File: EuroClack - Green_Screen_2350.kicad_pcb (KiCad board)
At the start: 4 copper layers, 99.1 x 110 mm, 272 parts, among them J1 C2982548, J10 CV_OUT_4, J11 C7471773, J12 DISPLAY_CONNECTOR, J13 CV_GATE_IN_4, J14 AUDIO_OUT_1, J15 AUDIO_IN_1, J16 USB_C_Receptacle_USB2.0_14P, J17 USB_HOST, J18 Eurorack 10 pin socket, J19 C7470101, J2 AUDIO_IN_2, J20 STEMMA_QT, J21 C2856837, J22 C2856837, J23 CV_GATE_IN3, J24 CV_GATE_IN_4, J25 SM03B-SRSS-TB, J26 CV_OUT_3, J27 CV_OUT_4, J28 C2881890, J29 C7470089, J3 CV_GATE_IN_1, J4 CV_GATE_IN_2, J5 CV_GATE_IN3, J6 AUDIO_OUT_2, J7 CV_OUT_1, J8 CV_OUT_2, J9 CV_OUT_3, Q1 A3400A, Q2 A3401A, Q3 A3401A, Q4 A3400A, SW3 RotaryEncoder_Switch, SW4 RotaryEncoder_Switch, SW5 USER2, SW6 SW_Push, SW7 SW_Push, U1 RP2350_80QFN, U10 SPX3819M5-L-5-0, U11 TL072, U12 TPS54302, U13 TL072, U14 SPX3819M5-L-3-3, U15 SRAM, U16 SPX3819M5-L-3-3, U17 TL072, U18 SN74LVC1T45DCK, U19 LM393, U2 PCM5102, U20 TL072, U21 LM393, U22 SN74LVC1T45DCK, U23 TPS54302, U3 MCP4728, U4 W25Q128JVS, U5 PCM1808PWR, U6 TL072, U7 REF3033, U8 TL072, U9 SPX3819M5-L-3-3, Y1 ABM8-272-T3

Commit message: work on connectors layout
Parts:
- removed the J12 at (225.0, 54.7)
- removed PIL1, PIL2, PIL3, PIL4: SMD_SMTSO20100CTJ, green_screen:SMD_SMTSO20100CTJ
- removed the REF** at (71.5, 111.0)
- removed the REF** at (113.5, 126.5)
- removed the REF** at (225.6, 93.9)
- removed the REF** at (256.1, 96.9)
- removed the REF** at (89.5, 126.5)
- removed the REF** at (30.0, 111.0)
- removed the REF** at (71.5, 55.5)
- removed the REF** at (30.0, 55.5)
- removed the REF** at (113.5, 150.6)
- added J30: FFC, green_screen:FPC-SMD_F1004-H-08-20G-R, F.Cu at (106.3, 59.6)
- added REF**: MountingHole_2.1mm, MountingHole:MountingHole_2.1mm, F.Cu at (88.4, 111.0)
- added REF**: MountingHole_2.1mm, MountingHole:MountingHole_2.1mm, F.Cu at (93.4, 126.6)
- added REF**: MountingHole_2.2mm_M2, MountingHole:MountingHole_2.2mm_M2, F.Cu at (71.5, 55.4)
- added REF**: MountingHole_2.1mm, MountingHole:MountingHole_2.1mm, F.Cu at (129.9, 111.0)
- added REF**: MountingHole_2.2mm_M2, MountingHole:MountingHole_2.2mm_M2, F.Cu at (30.0, 111.0)
- added REF**: MountingHole_2.1mm, MountingHole:MountingHole_2.1mm, F.Cu at (88.4, 55.5)
- added REF**: MountingHole_2.2mm_M2, MountingHole:MountingHole_2.2mm_M2, F.Cu at (106.2, 100.0)
- added REF**: MountingHole_2.2mm_M2, MountingHole:MountingHole_2.2mm_M2, F.Cu at (71.5, 111.0)
- added REF**: MountingHole_2.1mm, MountingHole:MountingHole_2.1mm, F.Cu at (119.3, 126.5)
- added REF**: MountingHole_2.1mm, MountingHole:MountingHole_2.1mm, F.Cu at (129.9, 55.5)
- added REF**: MountingHole_2.1mm, MountingHole:MountingHole_2.1mm, F.Cu at (119.3, 150.6)
- added REF**: MountingHole_2.2mm_M2, MountingHole:MountingHole_2.2mm_M2, F.Cu at (30.1, 55.6)
- J12: value DISPLAY_CONNECTOR -> Pin Header
- J16: footprint Clacktronics:918-418K2022Y40000 -> green_screen:USB-C-TH_TYPE-C-USB-14P
- J17: footprint Connector_USB:USB_A_Molex_105057_Vertical -> green_screen:USB-A-SMD_AF180-13.1
- SW3, SW4: footprint Rotary_Encoder:RotaryEncoder_Alps_EC12E-Switch_Vertical_H20mm_CircularMountingHoles -> green_screen:SW-TH_EC11XXXXXXXX
- SW5, SW6, SW7: footprint green_screen:KEY-SMD_4P-L6.0-W6.0-P3.90-LS9.0 -> green_screen:SW-TH_4P-L5.0-W5.0-P4.50-LS6.5
- moved REF** 121.2 mm to (88.4, 55.5), turned to 90 degrees
- moved J12 102.3 mm to (87.9, 78.5), turned to 180 degrees
- moved REF** 98.2 mm to (88.4, 83.7), turned to 90 degrees
- moved REF** 86.6 mm to (133.6, 55.5), turned to 90 degrees
- moved J16 55.0 mm to (133.0, 75.6)
- moved REF** 49.6 mm to (133.6, 83.7), turned to 90 degrees
- moved L4 48.7 mm to (108.5, 75.5)
- moved C36 34.3 mm to (107.9, 86.5)
- moved C87 34.3 mm to (112.8, 85.7)
- moved C88 34.3 mm to (106.6, 90.6)
- moved C85 34.3 mm to (106.6, 84.3)
- moved C86 34.3 mm to (106.6, 87.5)
- moved C89 34.3 mm to (106.6, 93.7)
- moved C98 34.3 mm to (108.0, 90.2)
- moved R98 34.3 mm to (114.9, 91.9)
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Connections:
- J22 pad 1: /AUDIO_IN_1_JACK -> /CV_OUT_1_JACK
- J22 pad 10: /USB_HOST_DM_JACK -> /ENC1_A_JACK
- J22 pad 11: /USB_DP_JACK -> /ENC1_SW_JACK
- J22 pad 12: /USB_DM_JACK -> /SW_USR2_JACK
- J22 pad 13: /GATE_OUT_1_JACK -> /SW_USR1_JACK
- J22 pad 14: /GATE_OUT_2_JACK -> /SW_RUN_JACK
- J22 pad 15: /CV_IN_1_JACK -> /~{SW_MENU_BOOT_JACK}
- J22 pad 16: /CV_IN_2_JACK -> /DISPLAY_BLK_JACK
- J22 pad 17: /12V_JACK -> /DISPLAY_RES_JACK
- J22 pad 18: /5V_JACK -> /DISPLAY_SDA_JACK
- J22 pad 19: /GND_JACK -> /DISPLAY_SCL_JACK
- J22 pad 2: /AUDIO_IN_2_JACK -> /CV_OUT_3_JACK
- J22 pad 20: /DISPLAY_DC_JACK -> /DISPLAY_CS_JACK
- J22 pad 21: /DISPLAY_CS_JACK -> /DISPLAY_DC_JACK
- J22 pad 22: /DISPLAY_SCL_JACK -> /GND_JACK
- J22 pad 23: /DISPLAY_SDA_JACK -> /5V_JACK
- J22 pad 24: /DISPLAY_RES_JACK -> /12V_JACK
- J22 pad 25: /DISPLAY_BLK_JACK -> /CV_IN_2_JACK
- J22 pad 26: /~{SW_MENU_BOOT_JACK} -> /CV_IN_1_JACK
- J22 pad 27: /SW_RUN_JACK -> /GATE_OUT_2_JACK
- J22 pad 28: /SW_USR1_JACK -> /GATE_OUT_1_JACK
- J22 pad 29: /SW_USR2_JACK -> /USB_DM_JACK
- J22 pad 3: /AUDIO_OUT_1_JACK -> /CV_OUT_4_JACK
- J22 pad 30: /ENC1_SW_JACK -> /USB_DP_JACK
- J22 pad 31: /ENC1_A_JACK -> /USB_HOST_DM_JACK
- J22 pad 32: /ENC1_B_JACK -> /USB_HOST_DP_JACK
- J22 pad 33: /ENC2_SW_JACK -> /GATE_IN_2_JACK
- J22 pad 34: /ENC2_A_JACK -> /GATE_IN_1_JACK
- J22 pad 35: /ENC2_B_JACK -> /CV_GATE_IN_4_JACK
- J22 pad 36: /~{USBH_PWR_EN_JACK} -> /CV_GATE_IN_3_JACK
- J22 pad 37: /CV_OUT_2_JACK -> /AUDIO_OUT_2_JACK
- J22 pad 38: /CV_OUT_4_JACK -> /AUDIO_OUT_1_JACK
- J22 pad 39: /CV_OUT_3_JACK -> /AUDIO_IN_2_JACK
- J22 pad 4: /AUDIO_OUT_2_JACK -> /CV_OUT_2_JACK
- J22 pad 40: /CV_OUT_1_JACK -> /AUDIO_IN_1_JACK
- J22 pad 5: /CV_GATE_IN_3_JACK -> /~{USBH_PWR_EN_JACK}
- J22 pad 6: /CV_GATE_IN_4_JACK -> /ENC2_B_JACK
- J22 pad 7: /GATE_IN_1_JACK -> /ENC2_A_JACK
- J22 pad 8: /GATE_IN_2_JACK -> /ENC2_SW_JACK
- J22 pad 9: /USB_HOST_DP_JACK -> /ENC1_B_JACK
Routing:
- net /DISPLAY_SCL_JACK: track 0.00 -> 37.5 mm, vias 0 -> 2
- net /DISPLAY_SDA_JACK: track 0.00 -> 36.7 mm, vias 0 -> 2
- net /DISPLAY_BLK_JACK: track 0.00 -> 36.5 mm, vias 0 -> 1
- net /DISPLAY_RES_JACK: track 0.00 -> 36.2 mm, vias 0 -> 2
- net /DISPLAY_CS_JACK: track 0.00 -> 33.8 mm, vias 0 -> 1
- net /DISPLAY_DC_JACK: track 0.00 -> 32.7 mm, vias 0 -> 1
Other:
- board size 99.1 x 110 mm -> 109.2 x 110 mm

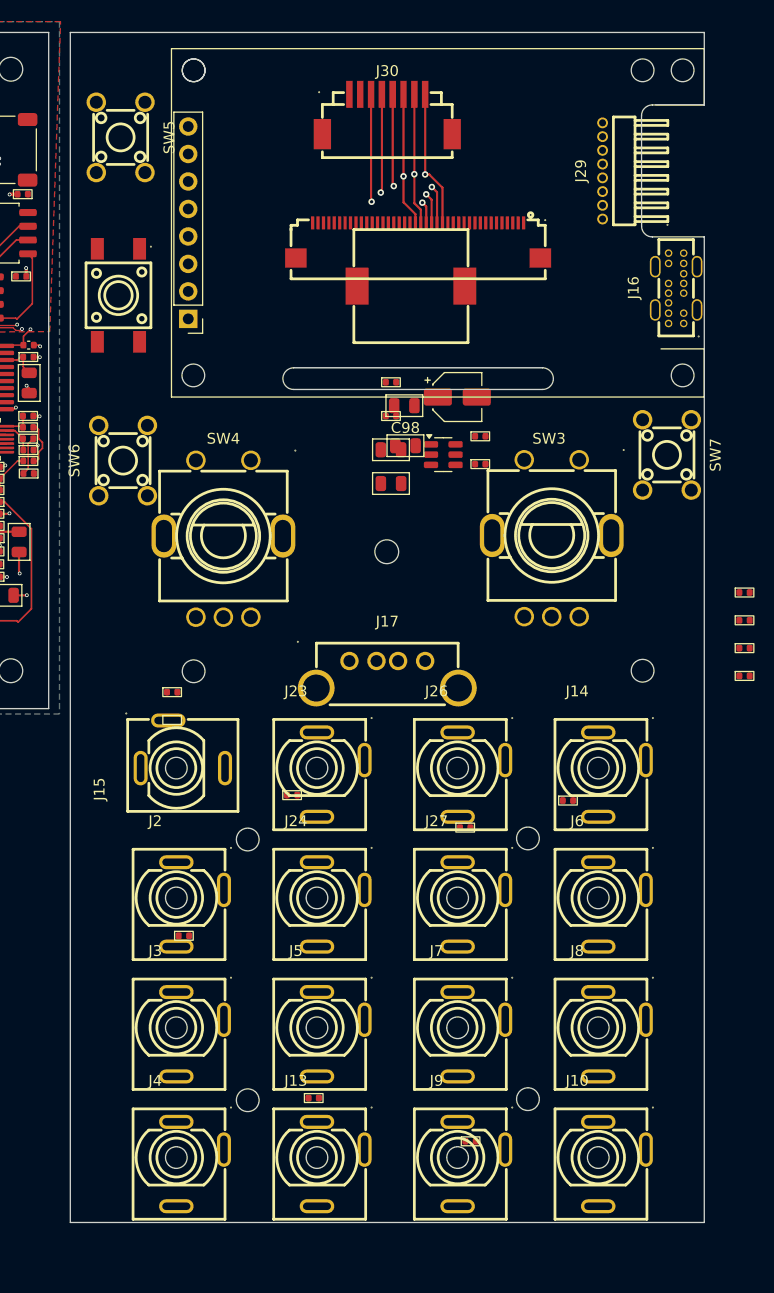
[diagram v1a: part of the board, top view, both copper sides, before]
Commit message: Added ground pour to panel and asjusted nets to suit
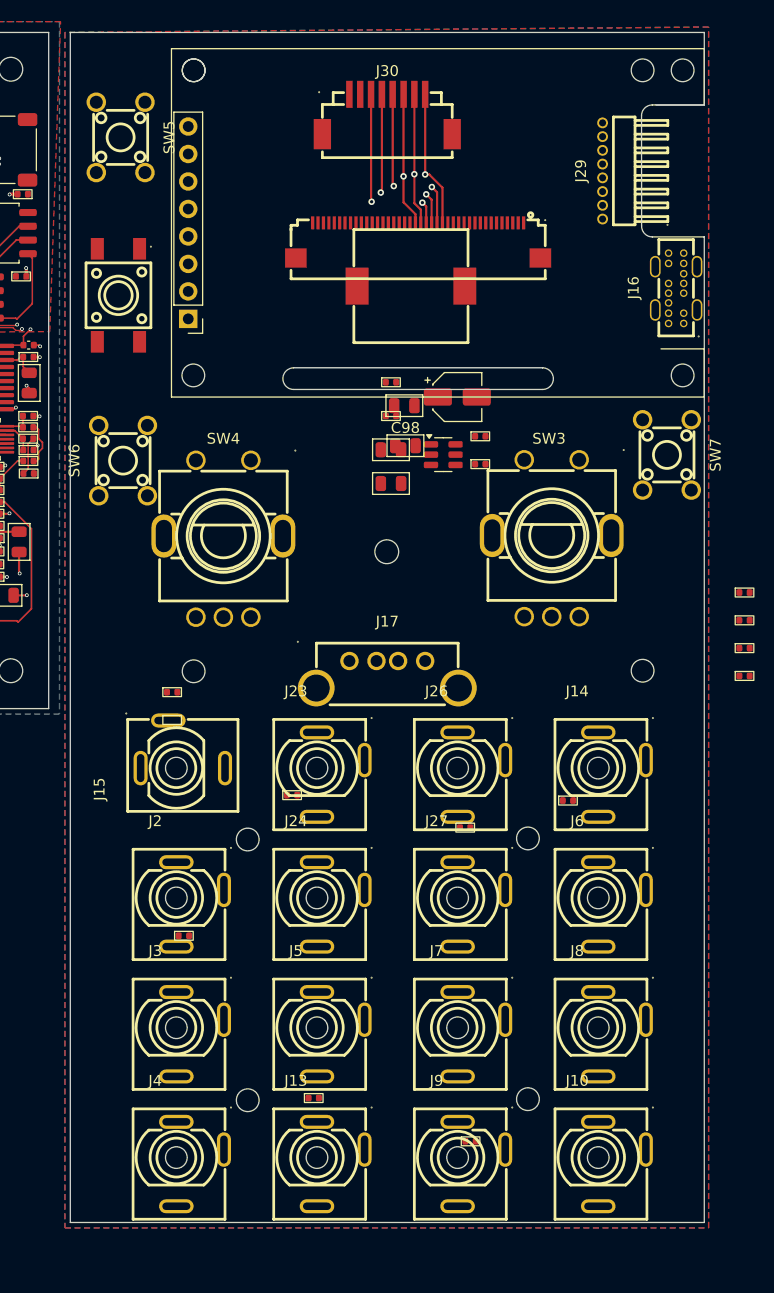
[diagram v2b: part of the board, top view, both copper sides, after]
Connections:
- J10 pad S: /GNDA_JACK -> /GND_JACK
- J26 pad S: /GNDA_JACK -> /GND_JACK
- J27 pad S: /GNDA_JACK -> /GND_JACK
- J7 pad S: /GNDA_JACK -> /GND_JACK
- J8 pad S: /GNDA_JACK -> /GND_JACK
- J9 pad S: /GNDA_JACK -> /GND_JACK
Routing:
- added copper zone on B.Cu, net /GND_JACK
- added copper zone on F.Cu, net /GND_JACK

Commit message: little bits
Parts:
- moved F1 46.6 mm to (102.5, 105.0), turned to -90 degrees
- moved Q3 37.9 mm to (105.9, 105.0)
- moved R99 36.8 mm to (102.5, 102.0)
- moved Q4 34.0 mm to (110.1, 105.0), turned to 180 degrees
- moved R102 33.6 mm to (106.0, 107.5)
- moved R101 30.8 mm to (108.5, 107.5), turned to 180 degrees
- moved R100 25.8 mm to (113.5, 106.0)
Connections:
- SW6 pad 1: GND -> /GND_JACK
- SW7 pad 1: GND -> /GND_JACK
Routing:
- net +5V: track 104.8 -> 115.1 mm
- net Net-(U12-FB): track 1.04 -> 4.89 mm
- net /QSPI_SCLK: track 28.1 -> 31.5 mm, vias 4 -> 6
- net /QSPI_SD3: track 28.3 -> 30.4 mm, vias 2 -> 4
- net Net-(D1-COM): track 2.91 -> 4.41 mm
- net GND: track 125.6 -> 125.4 mm, vias 115 -> 117

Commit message: Tweaks
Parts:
- moved U23 49.9 mm to (160.6, 82.4)
- moved C86 49.9 mm to (155.8, 78.8)
- moved C88 49.9 mm to (155.8, 81.9)
- moved R97 49.9 mm to (164.0, 80.7)
- moved R98 49.9 mm to (164.0, 83.3)
- moved C85 49.9 mm to (155.8, 75.7)
- moved C87 49.9 mm to (161.9, 77.1)
- moved C89 49.9 mm to (155.8, 85.1)
- moved L4 49.9 mm to (157.6, 66.8)
- moved R23 0.62 mm to (63.8, 62.9), turned to 90 degrees
- turned J15 to 0 degrees
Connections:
- C85 pad 1: GND -> /GND_JACK
- C87 pad 2: GND -> /GND_JACK
- C88 pad 2: GND -> /GND_JACK
- C89 pad 2: GND -> /GND_JACK
- R98 pad 1: GND -> /GND_JACK
- U23 pad 1: GND -> /GND_JACK
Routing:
- net /AUDIO_IN_2_JACK: track 0.00 -> 69.0 mm, vias 0 -> 1
- net /AUDIO_IN_1_JACK: track 0.00 -> 57.4 mm, vias 0 -> 1
- net /GATE_IN_1_JACK: track 0.00 -> 55.4 mm, vias 0 -> 1
- net /~{QSPI_SS}: track 6.32 -> 30.8 mm, vias 2 -> 4
- net /AUDIO_R_IN: track 1.00 -> 18.8 mm, vias 0 -> 2
- net /~{SW_MENU_BOOT_MICRO}: track 52.7 -> 68.5 mm, vias 2 -> 3
- net +5VA: track 11.5 -> 20.6 mm, vias 0 -> 2
- net +12V: track 172.7 -> 176.1 mm
- net GND: track 125.4 -> 124.0 mm, vias 117 -> 118
- net /QSPI_SD1: track 16.3 -> 15.7 mm
- net +1V1: track 24.9 -> 25.0 mm, vias 24 -> 9
